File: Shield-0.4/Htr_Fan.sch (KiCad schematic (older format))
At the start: 31 parts, among them J27 TP

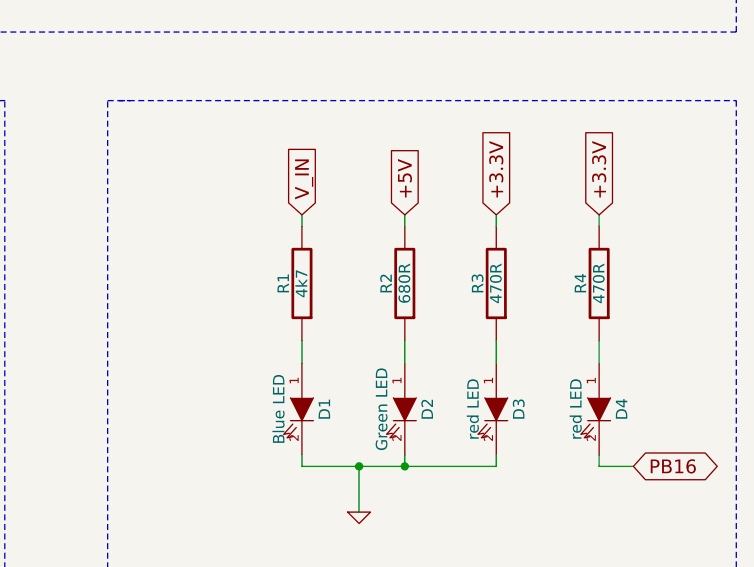
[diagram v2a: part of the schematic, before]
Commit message: Duet 0.8 power voltage test points added.  Ballast resistors on power LEDs changed to make each the same brightness (allowing for the fact that the human eye sees green as a lot brighter than blue or red).
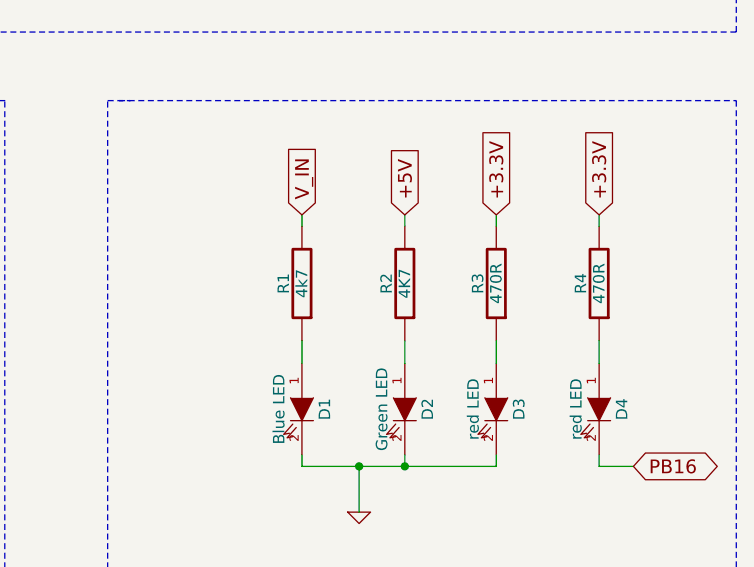
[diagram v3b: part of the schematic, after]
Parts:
- R2: value 680R -> 4K7
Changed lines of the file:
@@
 P 7100 5850
 F 0 "R2" V 7180 5850 50  0000 C CNN
-F 1 "680R" V 7100 5850 50  0000 C CNN
+F 1 "4K7" V 7100 5850 50  0000 C CNN
 F 2 "" H 7100 5850 60  0001 C CNN
 F 3 "" H 7100 5850 60  0001 C CNN

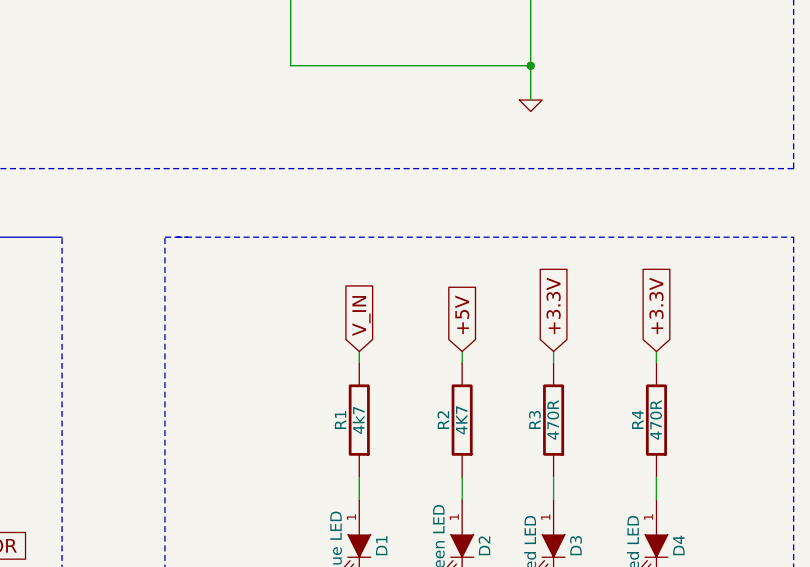
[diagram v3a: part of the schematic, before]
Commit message: Voltage test points added to Shield.
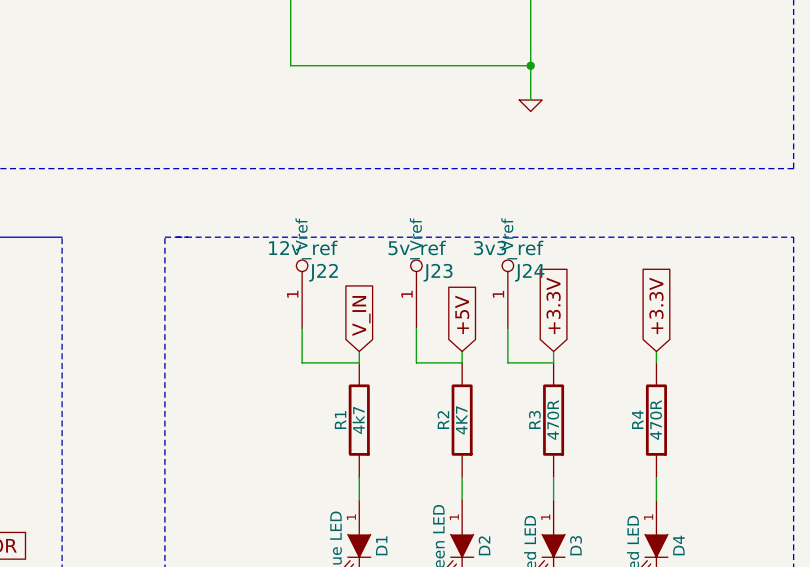
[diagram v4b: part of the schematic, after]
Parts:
- added J22: 12v_ref, ~, symbol VREF
- added J23: 5v_ref, ~, symbol VREF
- added J24: 3v3_ref, ~, symbol VREF
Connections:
- net +3.3V: now also J24.1 (Vref)
- net +5V: now also J23.1 (Vref)
- net V_IN: now also J22.1 (Vref)
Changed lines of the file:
@@
 Wire Wire Line
 	8100 6650 7950 6650
+$Comp
+L VREF J24
+U 1 1 559E5F05
+P 7300 5450
+F 0 "J24" H 7400 5700 60  0000 C CNN
+F 1 "3v3_ref" H 7300 5800 60  0000 C CNN
+F 2 "~" H 7300 5450 60  0000 C CNN
+F 3 "~" H 7300 5450 60  0000 C CNN
+	1    7300 5450
+	1    0    0    -1
+$EndComp
+$Comp
+L VREF J23
+U 1 1 559E5F14
+P 6900 5450
+F 0 "J23" H 7000 5700 60  0000 C CNN
+F 1 "5v_ref" H 6900 5800 60  0000 C CNN
+F 2 "~" H 6900 5450 60  0000 C CNN
+F 3 "~" H 6900 5450 60  0000 C CNN
+	1    6900 5450
+	1    0    0    -1
+$EndComp
+$Comp
+L VREF J22
+U 1 1 559E5F23
+P 6400 5450
+F 0 "J22" H 6500 5700 60  0000 C CNN
+F 1 "12v_ref" H 6400 5800 60  0000 C CNN
+F 2 "~" H 6400 5450 60  0000 C CNN
+F 3 "~" H 6400 5450 60  0000 C CNN
+	1    6400 5450
+	1    0    0    -1
+$EndComp
+Wire Wire Line
+	7300 5450 7300 5600
+Wire Wire Line
+	7300 5600 7500 5600
+Wire Wire Line
+	6900 5450 6900 5600
+Wire Wire Line
+	6900 5600 7100 5600
+Wire Wire Line
+	6400 5450 6400 5600
+Wire Wire Line
+	6400 5600 6650 5600
 $EndSCHEMATC
